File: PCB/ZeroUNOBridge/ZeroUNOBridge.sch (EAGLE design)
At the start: 19 parts, among them J1 RASPBERRYPI-40-PIN-GPIO, U1 ATMEGA328P_PDIP_EZ

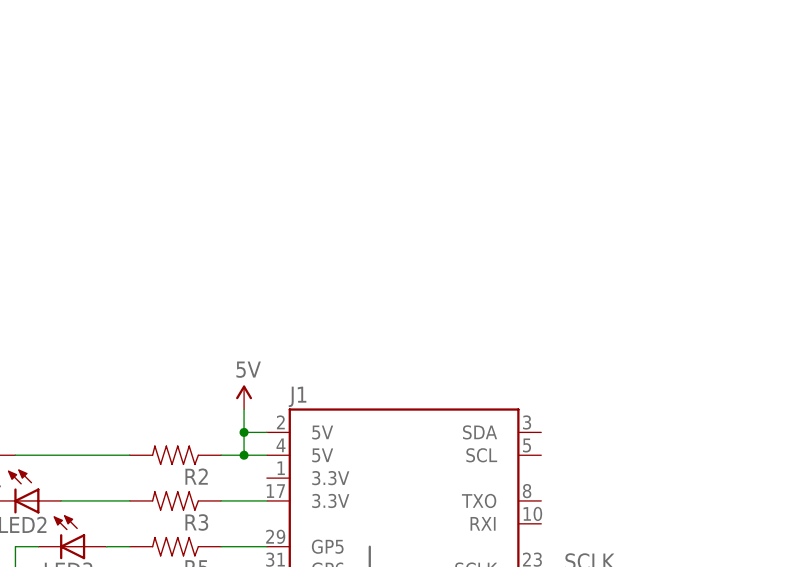
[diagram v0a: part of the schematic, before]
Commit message: Added Power Jack
-Changed RPi port to compensate
-Adjusted labels
-Added tag
-Added initials
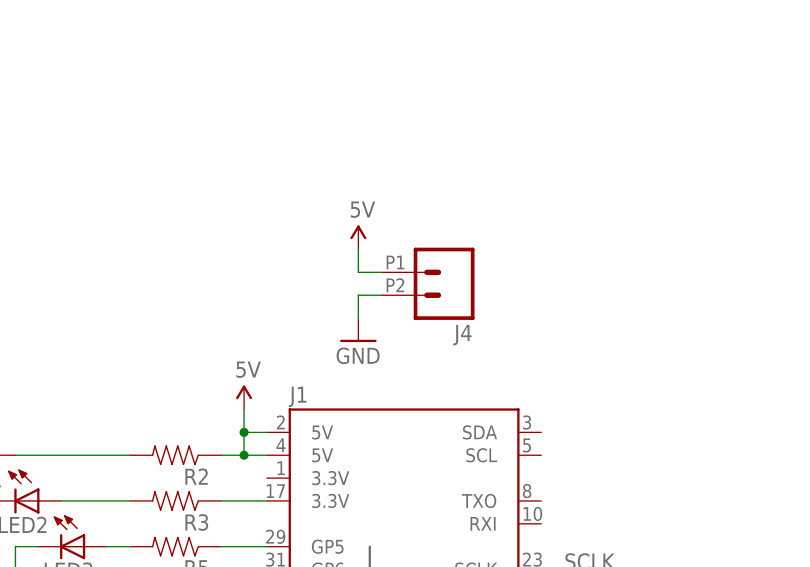
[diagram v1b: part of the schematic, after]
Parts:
- added J4: (no value), SparkFun-Connectors:M022.54MM_SCREWTERM
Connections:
- removed net N$8: LED4.C
- net 5V: now also J4.1
- net GND: now also J4.2, LED4.C
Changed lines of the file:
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@@
 <part name="LED3" library="adafruit" deviceset="LED" device="5MM"/>
 <part name="LED4" library="adafruit" deviceset="LED" device="5MM"/>
-<part name="GND8" library="SparkFun-Aesthetics" deviceset="GND" device=""/>
 <part name="R7" library="SparkFun-Sensors" deviceset="PHOTOCELL" device="PTH"/>
 <part name="R8" library="SparkFun-Resistors" deviceset="RESISTOR" device="PTH-1/4W"/>
 <part name="GND9" library="SparkFun-Aesthetics" deviceset="GND" device=""/>
 <part name="SUPPLY3" library="SparkFun-Aesthetics" deviceset="5V" device=""/>
+<part name="J4" library="SparkFun-Connectors" deviceset="M02" device="2.54MM_SCREWTERM"/>
+<part name="SUPPLY4" library="SparkFun-Aesthetics" deviceset="5V" device=""/>
+<part name="GND10" library="SparkFun-Aesthetics" deviceset="GND" device=""/>
+<part name="GND8" library="SparkFun-Aesthetics" deviceset="GND" device=""/>
 </parts>
 <sheets>
@@
 <instance part="LED3" gate="G$1" x="-10.16" y="104.14" rot="R270"/>
 <instance part="LED4" gate="G$1" x="170.18" y="88.9" rot="R90"/>
-<instance part="GND8" gate="1" x="177.8" y="83.82"/>
 <instance part="R7" gate="G$1" x="149.86" y="116.84" smashed="yes" rot="R180">
 <attribute name="NAME" x="154.94" y="113.792" size="1.778" layer="95" rot="R180"/>
@@
 <instance part="GND9" gate="1" x="160.02" y="111.76"/>
 <instance part="SUPPLY3" gate="G$1" x="139.7" y="132.08"/>
+<instance part="J4" gate="G$1" x="30.48" y="134.62" rot="R180"/>
+<instance part="SUPPLY4" gate="G$1" x="20.32" y="137.16"/>
+<instance part="GND10" gate="1" x="20.32" y="127"/>
+<instance part="GND8" gate="1" x="177.8" y="83.82"/>
 </instances>
 <busses>
@@
 <wire x1="160.02" y1="116.84" x2="160.02" y2="114.3" width="0.1524" layer="91"/>
 </segment>
+<segment>
+<pinref part="GND10" gate="1" pin="GND"/>
+<wire x1="20.32" y1="129.54" x2="20.32" y2="132.08" width="0.1524" layer="91"/>
+<pinref part="J4" gate="G$1" pin="2"/>
+<wire x1="20.32" y1="132.08" x2="22.86" y2="132.08" width="0.1524" layer="91"/>
+</segment>
+<segment>
+<pinref part="LED4" gate="G$1" pin="C"/>
+<wire x1="175.26" y1="88.9" x2="177.8" y2="88.9" width="0.1524" layer="91"/>
+<wire x1="177.8" y1="88.9" x2="177.8" y2="86.36" width="0.1524" layer="91"/>
+<pinref part="GND8" gate="1" pin="GND"/>
+</segment>
 </net>
 <net name="5V" class="0">
@@
 <wire x1="139.7" y1="132.08" x2="139.7" y2="129.54" width="0.1524" layer="91"/>
 </segment>
+<segment>
+<pinref part="SUPPLY4" gate="G$1" pin="5V"/>
+<wire x1="20.32" y1="137.16" x2="20.32" y2="134.62" width="0.1524" layer="91"/>
+<pinref part="J4" gate="G$1" pin="1"/>
+<wire x1="20.32" y1="134.62" x2="22.86" y2="134.62" width="0.1524" layer="91"/>
+</segment>
 </net>
 <net name="RESET" class="0">
@@
 </segment>
 </net>
-<net name="N$8" class="0">
-<segment>
-<pinref part="LED4" gate="G$1" pin="C"/>
-<wire x1="175.26" y1="88.9" x2="177.8" y2="88.9" width="0.1524" layer="91"/>
-<wire x1="177.8" y1="88.9" x2="177.8" y2="86.36" width="0.1524" layer="91"/>
-<pinref part="GND8" gate="1" pin="GND"/>
-</segment>
-</net>

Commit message: Final Labeling Corrections
-Labeling jacks
-Added tag
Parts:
- removed FRAME1: FRAME-LEDGER, SparkFun-Aesthetics:FRAME-LEDGER
- J1: value RASPBERRYPI-40-PIN-GPIO -> (none); device SparkFun-Boards:RASPBERRYPI-40-PIN-GPIO -> SparkFun-Connectors:M022.54MM_SCREWTERM
- J2: device SparkFun-Connectors:M05SCREW -> SparkFun-Connectors:M022.54MM_SCREWTERM
- J3: value (none) -> RASPBERRYPI-40-PIN-GPIO; device SparkFun-Connectors:M022.54MM_SCREWTERM -> SparkFun-Boards:RASPBERRYPI-40-PIN-GPIO
- J4: device SparkFun-Connectors:M022.54MM_SCREWTERM -> SparkFun-Connectors:M05SCREW
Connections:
- net 5V: now also J1.1, J3.5V@2, J3.5V@4, R1.1, R3.2; no longer J1.5V@2, J1.5V@4, J4.1, R2.1, R4.2
- net GND: now also J1.2, J3.GND@14, J3.GND@20, J3.GND@25, J3.GND@30, J3.GND@34, J3.GND@39, J3.GND@6, J3.GND@9; no longer J1.GND@14, J1.GND@20, J1.GND@25, J1.GND@30, J1.GND@34, J1.GND@39, J1.GND@6, J1.GND@9, J4.2
- net MISO: now also J3.MISO; no longer J1.MISO
- net MOSI: now also J3.MOSI; no longer J1.MOSI
- net N$1: now also J3.3.3V@17, R2.1; no longer J1.3.3V@17, R3.1
- net N$2: now also J3.GP5, R4.1; no longer J1.GP5, R5.1
- net N$3: now also R1.2; no longer R2.2
- net N$4: now also R2.2; no longer R3.2
- net N$5: now also R4.2; no longer R5.2
- net N$6: now also R5.1; no longer R6.1
- net N$7: now also R5.2; no longer R6.2
- net PIN10~: now also J4.5; no longer J2.5
- net PIN3~: now also J4.1; no longer J2.1
- net PIN5~: now also J4.2; no longer J2.2
- net PIN6~: now also J4.3; no longer J2.3
- net PIN9~: now also J4.4; no longer J2.4
- net RESET: now also J3.GP25, R3.1; no longer J1.GP25, R4.1
- net RX: now also J2.1; no longer J3.1
- net SCLK: now also J3.SCLK; no longer J1.SCLK
- net TX: now also J2.2; no longer J3.2
- net XTAL1: now also R6.2; no longer R1.2
- net XTAL2: now also R6.1; no longer R1.1
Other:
- moved on the sheet: R1, R2, R3, R4, R5, R6

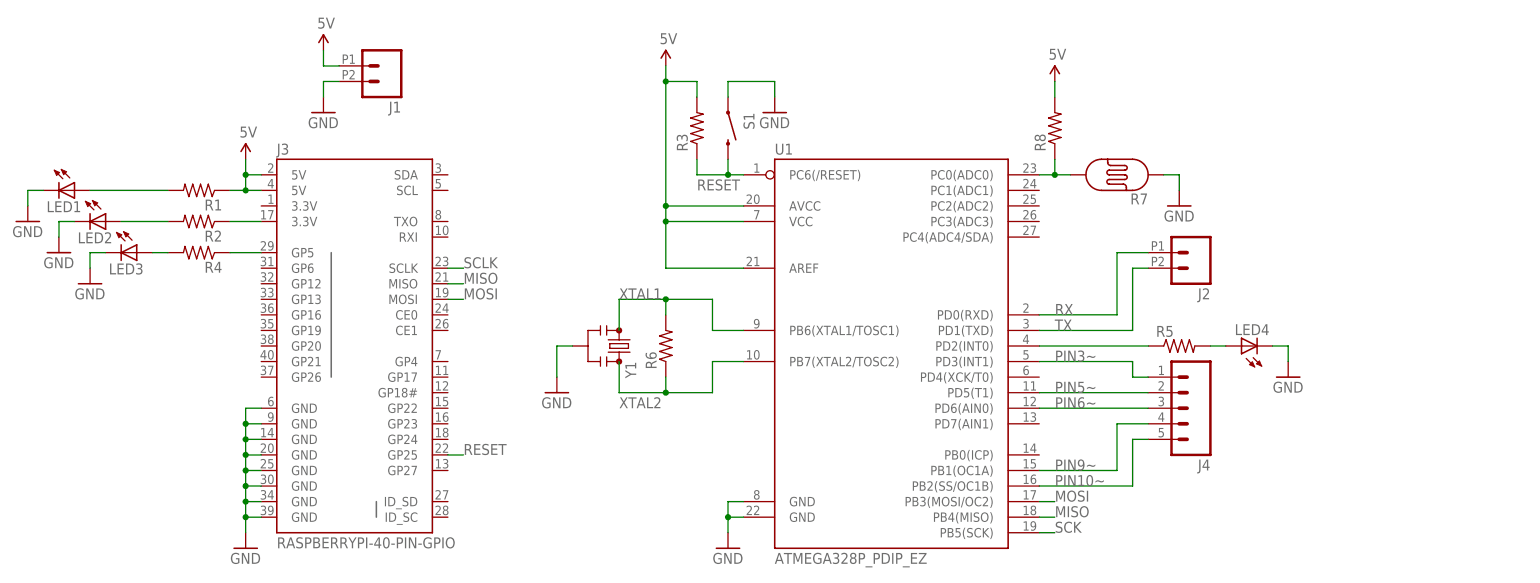
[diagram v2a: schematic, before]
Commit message: Misc Fixes
-Made board dimensions smaller
-Moved Bri's tag
-Actually connected up the SPI clock
-Moved 3.3V LED to other 3.3V port on RPi header
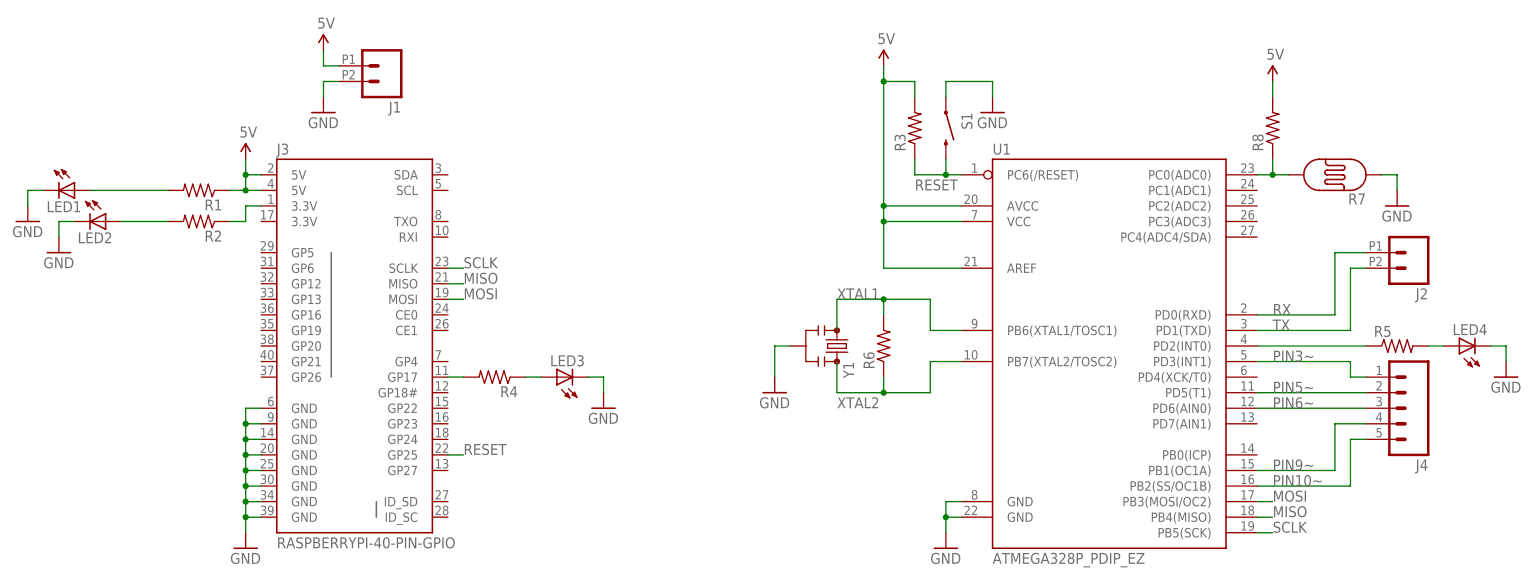
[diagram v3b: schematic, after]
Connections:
- removed net SCK: U1.PB5(SCK)
- net N$1: now also J3.3.3V@1; no longer J3.3.3V@17
- net N$2: now also J3.GP17, R4.2; no longer J3.GP5, R4.1
- net N$5: now also R4.1; no longer R4.2
- net SCLK: now also U1.PB5(SCK)
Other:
- moved on the sheet: J2, J4, LED3, LED4, R3, R4, R5, R6, R7, R8, S1, U1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

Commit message: Added level translators so the RPi doesn't blow up
pretty much redid the entire thing - many conversions to SMD
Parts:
- removed J2: (no value), SparkFun-Connectors:M022.54MM_SCREWTERM
- added FRAME1: FRAME-LEDGER, SparkFun-Aesthetics:FRAME-LEDGER
- added Q1, Q2, Q3, Q4, Q5, Q6: BSS138, SparkFun-DiscreteSemi:MOSFET-NCHANNELBSS138
- added R10, R11, R12, R13, R14, R15, R16, R17, R18, R19, R20, R9: 10K, SparkFun-Resistors:10KOHM-1/10W-1%(0603)0603
- LED1: value (none) -> RED; device adafruit:LED5MM -> SparkFun-LED:LED-RED0603
- LED2: value (none) -> Yellow; device adafruit:LED5MM -> SparkFun-LED:LED-YELLOW0603
- LED3: value (none) -> BLUE; device adafruit:LED5MM -> SparkFun-LED:LED-BLUE0603
- LED4: value (none) -> GREEN; device adafruit:LED5MM -> SparkFun-LED:LED-GREEN0603
- R1, R2, R4, R5: value (none) -> 330; device SparkFun-Resistors:RESISTORPTH-1/4W -> SparkFun-Resistors:330OHM1/10W1%(0603)
- R3, R8: value (none) -> 10K; device SparkFun-Resistors:RESISTORPTH-1/4W -> SparkFun-Resistors:10KOHM-1/10W-1%(0603)0603
- R6: value (none) -> 1M; device SparkFun-Resistors:RESISTORPTH-1/4W -> SparkFun-Resistors:1MOHM-1/10W-1%(0603)
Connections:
- removed net MISO: J3.MISO, U1.PB4(MISO)
- removed net MOSI: J3.MOSI, U1.PB3(MOSI/OC2)
- removed net N$2: J3.GP17, R4.2
- removed net RESET: J3.GP25, R3.1, S1.2, U1.PC6(/RESET)
- removed net RX: J2.1, U1.PD0(RXD)
- removed net SCLK: J3.SCLK, U1.PB5(SCK)
- removed net TX: J2.2, U1.PD1(TXD)
- new net 3.3V: J3.3.3V@1, Q1.G, Q2.G, Q3.G, Q4.G, Q5.G, Q6.G, R11.2, R13.2, R15.2, R17.2, R19.2, R2.1, R9.2
- new net MISO_HV: Q5.D, R18.1, U1.PB4(MISO)
- new net MISO_LV: J3.MISO, Q5.S, R17.1
- new net MOSI_HV: Q4.D, R16.1, U1.PB3(MOSI/OC2)
- new net MOSI_LV: J3.MOSI, Q4.S, R15.1
- new net RESET_HV: Q6.D, R20.1, R3.1, S1.2, U1.PC6(/RESET)
- new net RESET_LV: J3.GP25, Q6.S, R19.1
- new net RX_HV: Q1.D, R10.1, U1.PD0(RXD)
- new net RX_LV: J3.RXI, Q2.S, R11.1
- new net SCLK_HV: Q3.D, R14.1, U1.PB5(SCK)
- new net SCLK_LV: J3.SCLK, Q3.S, R13.1
- new net TX_HV: Q2.D, R12.1, U1.PD1(TXD)
- new net TX_LV: J3.TXO, Q1.S, R9.1
- net 5V: now also R10.2, R12.2, R14.2, R16.2, R18.2, R20.2
- net N$1: now also J3.GP26, R4.2; no longer J3.3.3V@1, R2.1
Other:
- moved on the sheet: R1, R2, R3, R4, R5

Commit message: Final Changes
-DRC clear
-Renumber
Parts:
- removed J4: (no value), SparkFun-Connectors:M05SCREW
- added J2: RASPBERRYPI-40-PIN-GPIO, SparkFun-Boards:RASPBERRYPI-40-PIN-GPIO
- J3: value RASPBERRYPI-40-PIN-GPIO -> (none); device SparkFun-Boards:RASPBERRYPI-40-PIN-GPIO -> SparkFun-Connectors:M05SCREW
- LED3: value BLUE -> GREEN; device SparkFun-LED:LED-BLUE0603 -> SparkFun-LED:LED-GREEN0603
- LED4: value GREEN -> BLUE; device SparkFun-LED:LED-GREEN0603 -> SparkFun-LED:LED-BLUE0603
- R10: value 10K -> PHOTOCELLPTH; device SparkFun-Resistors:10KOHM-1/10W-1%(0603)0603 -> SparkFun-Sensors:PHOTOCELLPTH
- R16: value 10K -> 1M; device SparkFun-Resistors:10KOHM-1/10W-1%(0603)0603 -> SparkFun-Resistors:1MOHM-1/10W-1%(0603)
- R20, R8: value 10K -> 330; device SparkFun-Resistors:10KOHM-1/10W-1%(0603)0603 -> SparkFun-Resistors:330OHM1/10W1%(0603)
- R4, R5: value 330 -> 10K; device SparkFun-Resistors:330OHM1/10W1%(0603) -> SparkFun-Resistors:10KOHM-1/10W-1%(0603)0603
- R6: value 1M -> 10K; device SparkFun-Resistors:1MOHM-1/10W-1%(0603) -> SparkFun-Resistors:10KOHM-1/10W-1%(0603)0603
- R7: value PHOTOCELLPTH -> 10K; device SparkFun-Sensors:PHOTOCELLPTH -> SparkFun-Resistors:10KOHM-1/10W-1%(0603)0603
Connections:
- net 3.3V: now also J2.3.3V@1, R14.2, R5.2, R7.2; no longer J3.3.3V@1, R13.2, R15.2, R9.2
- net 5V: now also J2.5V@2, J2.5V@4, R13.2, R15.2, R4.2, R6.2, R9.2; no longer J3.5V@2, J3.5V@4, R10.2, R14.2, R16.2, R20.2, R8.2
- net GND: now also J2.GND@14, J2.GND@20, J2.GND@25, J2.GND@30, J2.GND@34, J2.GND@39, J2.GND@6, J2.GND@9, R10.P$1; no longer J3.GND@14, J3.GND@20, J3.GND@25, J3.GND@30, J3.GND@34, J3.GND@39, J3.GND@6, J3.GND@9, R7.P$1
- net MISO_HV: now also Q6.D; no longer Q5.D
- net MISO_LV: now also J2.MISO, Q6.S, R19.1; no longer J3.MISO, Q5.S, R17.1
- net MOSI_HV: now also R13.1; no longer R16.1
- net MOSI_LV: now also J2.MOSI, R14.1; no longer J3.MOSI, R15.1
- net N$1: now also J2.GP26, R20.2; no longer J3.GP26, R4.2
- net N$5: now also LED4.A, R20.1; no longer LED3.A, R4.1
- net N$6: now also R8.1; no longer R5.1
- net N$7: now also LED3.A, R8.2; no longer LED4.A, R5.2
- net N$9: now also R10.P$2, R12.1; no longer R7.P$2, R8.1
- net PIN10~: now also J3.5; no longer J4.5
- net PIN3~: now also J3.1; no longer J4.1
- net PIN5~: now also J3.2; no longer J4.2
- net PIN6~: now also J3.3; no longer J4.3
- net PIN9~: now also J3.4; no longer J4.4
- net RESET_HV: now also Q1.D, R4.1; no longer Q6.D, R20.1
- net RESET_LV: now also J2.GP25, Q1.S, R5.1; no longer J3.GP25, Q6.S, R19.1
- net RX_HV: now also Q2.D, R6.1; no longer Q1.D, R10.1
- net RX_LV: now also J2.RXI, Q3.S; no longer J3.RXI, Q2.S
- net SCLK_HV: now also Q5.D, R15.1; no longer Q3.D, R14.1
- net SCLK_LV: now also J2.SCLK, Q5.S, R17.1; no longer J3.SCLK, Q3.S, R13.1
- net TX_HV: now also Q3.D, R9.1; no longer Q2.D, R12.1
- net TX_LV: now also J2.TXO, Q2.S, R7.1; no longer J3.TXO, Q1.S, R9.1
- net XTAL1: now also R16.2; no longer R6.2
- net XTAL2: now also R16.1; no longer R6.1
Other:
- moved on the sheet: LED3, LED4, Q1, Q2, Q3, Q5, Q6, R12, R13, R14, R15, R16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
